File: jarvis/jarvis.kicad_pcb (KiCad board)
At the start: 4 copper layers, 52 x 29.4 mm, 74 parts, among them IC1 ESP32-S3R16V, IC2 MAX98357AETE+T, IC3 MCP73871T-4CAI_ML, IC4 TLV70033DDCT, IC5 W25Q128JWSIQ, J1 Conn_01x02 - Speaker, J2 Mic Conn_01x05, J3 Conn_01x02 - Battery, U1 TPD4E05U06QDQARQ1, U2 2137160001, Y2 ABM10W-40.0000MHZ-8-N1G-T3, Y3 ECS-.327-12.5-1210B-N-TR

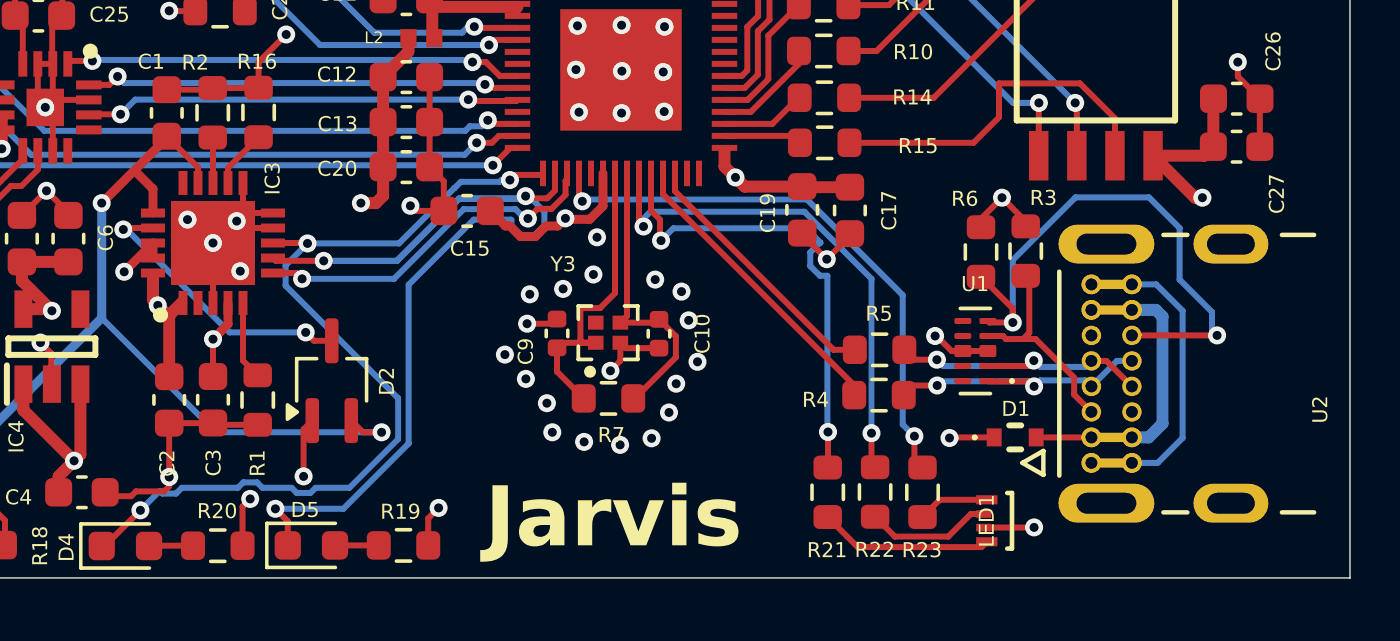
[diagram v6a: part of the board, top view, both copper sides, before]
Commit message: small fixes from testing new pcb swap d lines connected pins on power ic that needed to be changed rbg led to be common anode
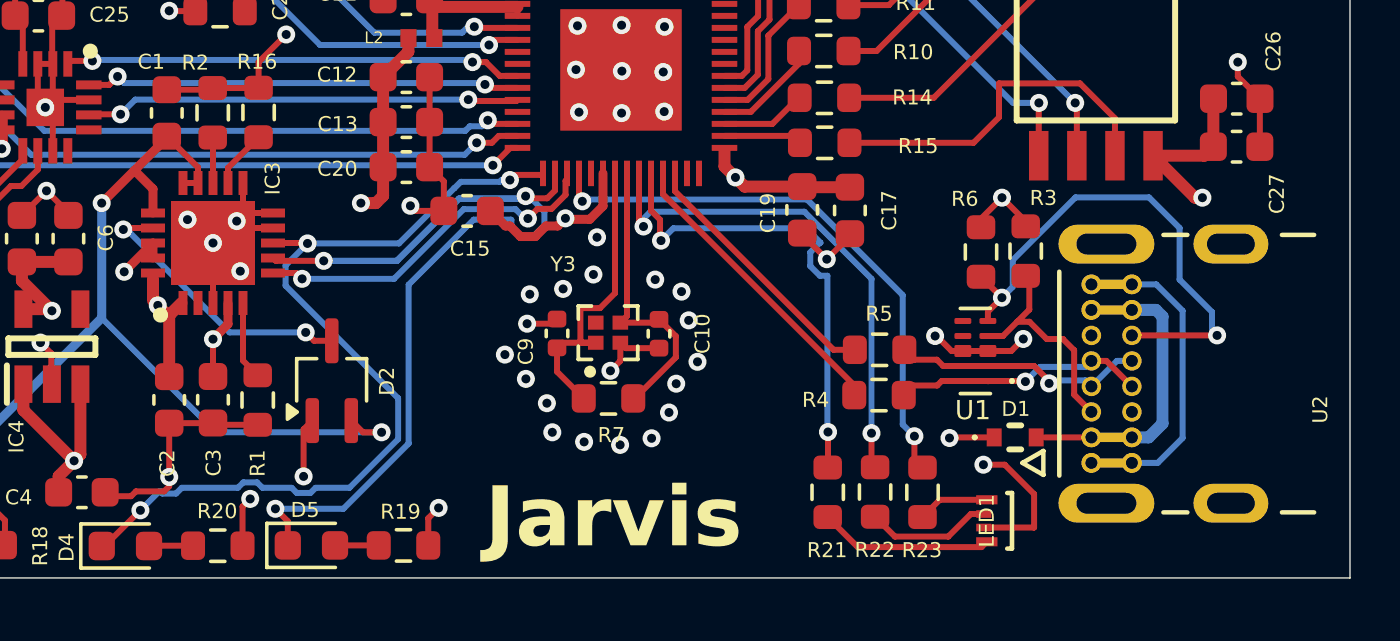
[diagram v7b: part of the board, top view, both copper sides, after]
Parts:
- R16: value 2k -> 20k
- S1: value EVQ-P9H02W -> EVQ-P9H02W reset
- U1: footprint jarvis:IC_TPD4E05U06QDQARQ1 -> jarvis:IC_TPD4E05U06QDQARQ1-two
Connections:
- LED1 pad 2: GND -> +3.3V
- R4 pad 1: /Power/USB_DP -> /Power/USB_DN
- R5 pad 1: /Power/USB_DN -> /Power/USB_DP
- U1 pad 1: /Power/USB_DP -> /Power/USB_DN
- U1 pad 2: /Power/USB_DN -> /Power/USB_DP
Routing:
- net +3.3V: track 74.1 -> 98.3 mm, vias 12 -> 13
- net /Power/USB_DN: track 10.0 -> 8.45 mm, vias 2 -> 1
- net Net-(U2-CC2): track 18.8 -> 17.2 mm
- net /Power/USB_DP: track 10.00 -> 8.51 mm, vias 2 -> 1
- net /Power/VBAT_1: track 31.9 -> 32.4 mm
